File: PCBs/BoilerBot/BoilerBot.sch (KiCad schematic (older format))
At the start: 24 parts, among them J1 Screw_Terminal_01x02, J10 Conn_01x03_Male, J2 Screw_Terminal_01x03, J3 Screw_Terminal_01x03, J4 Screw_Terminal_01x02, J5 Conn_01x05_Male, J6 Conn_01x03_Male, J7 Conn_01x03_Male, J8 Screw_Terminal_01x03, J9 Conn_01x04_Male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

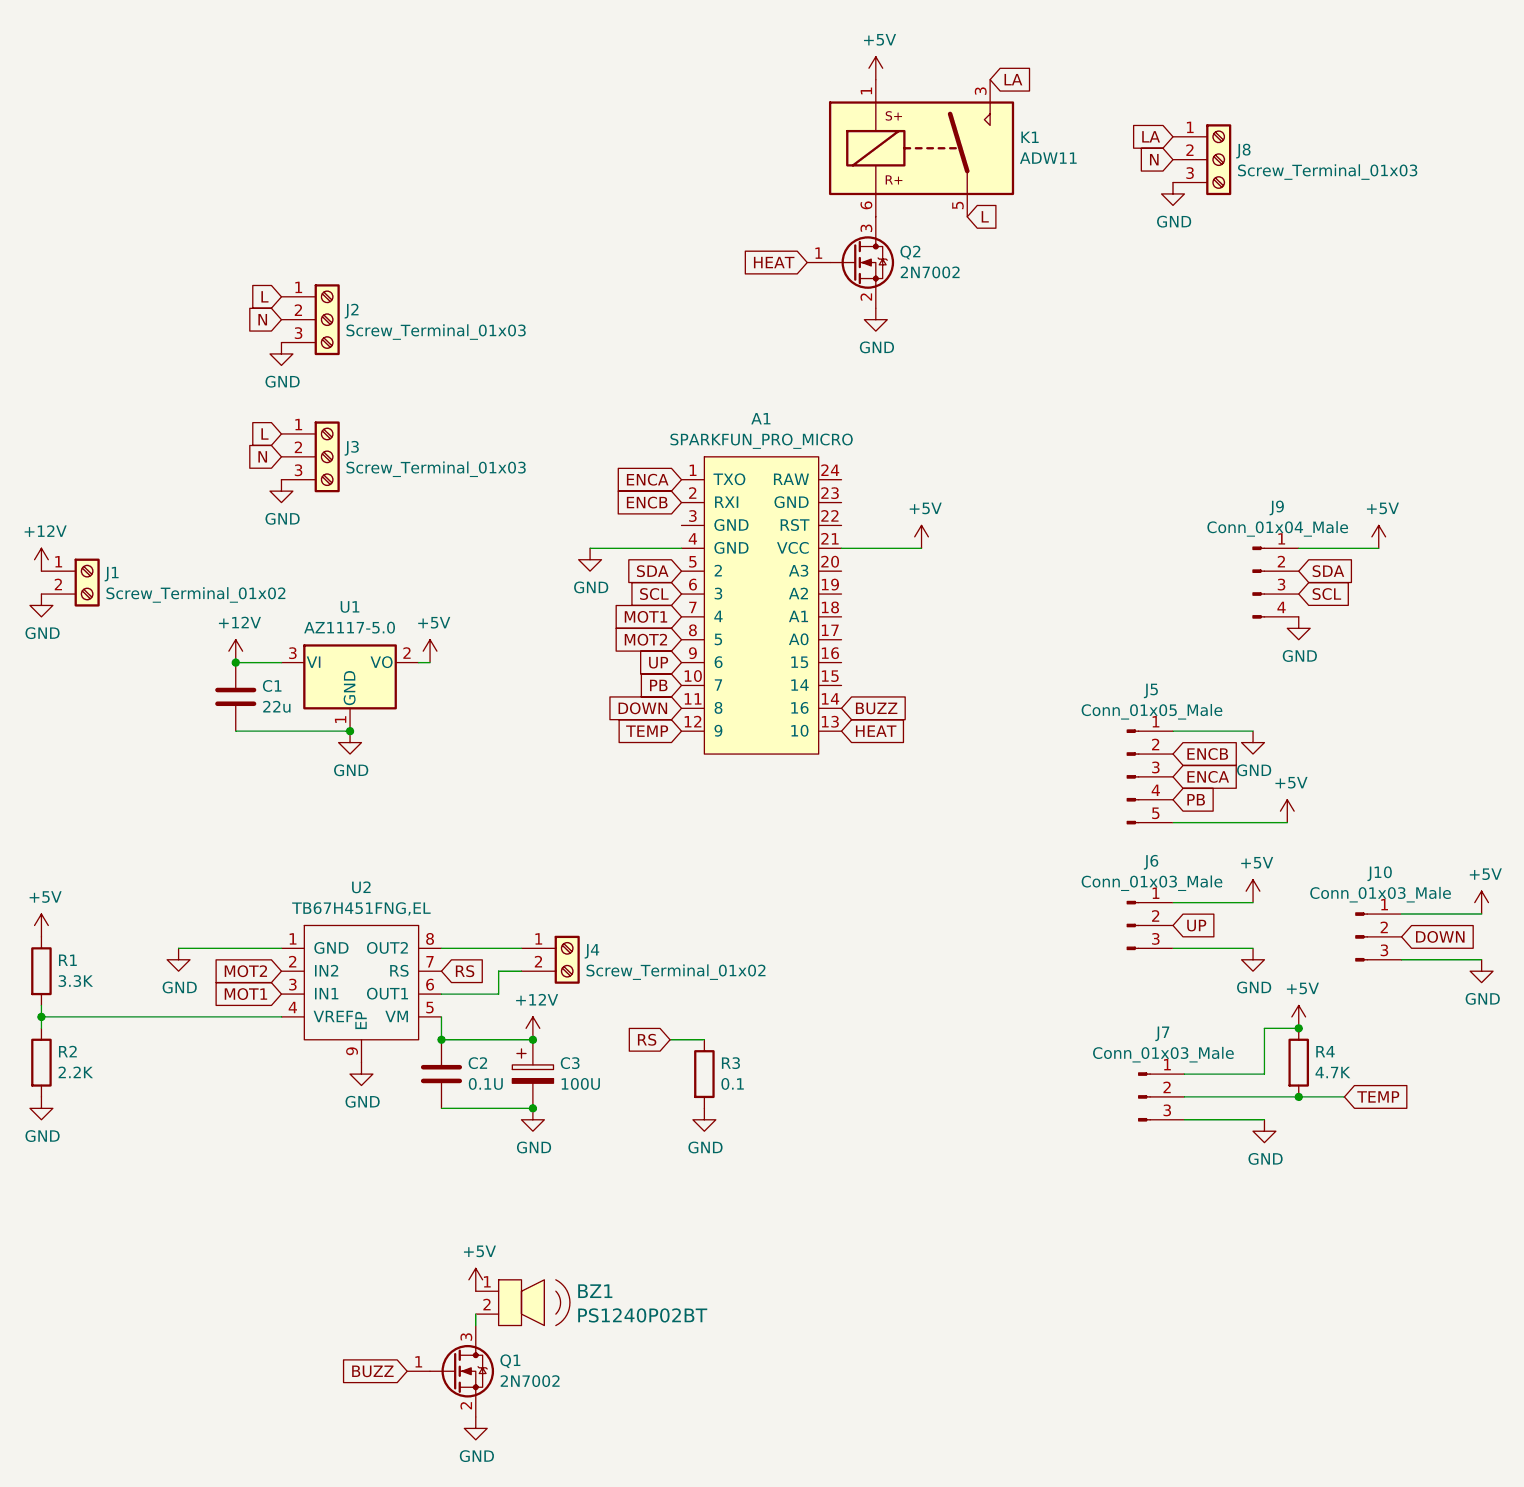
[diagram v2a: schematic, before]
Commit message: updates for off board PDB
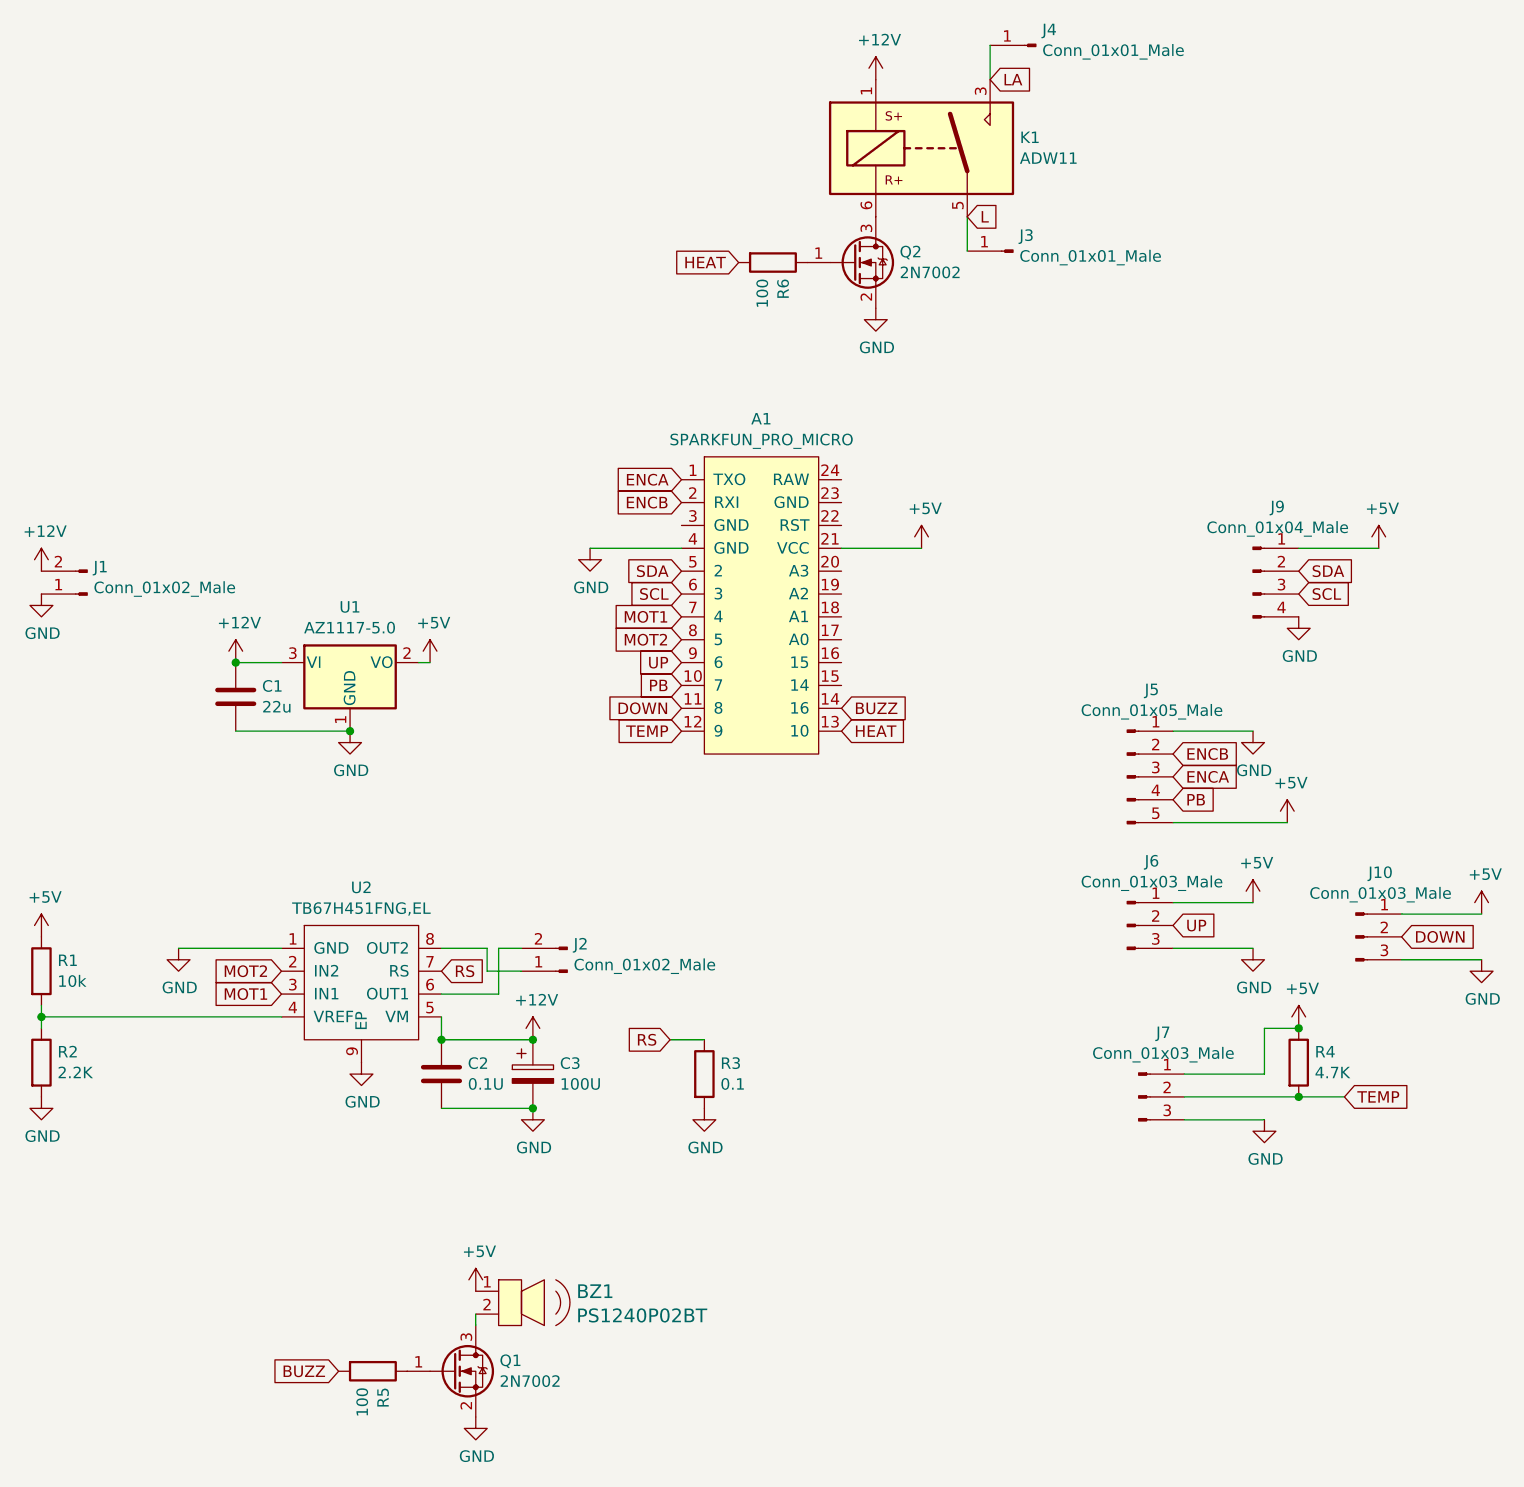
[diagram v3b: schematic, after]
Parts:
- removed J1, J4: Screw_Terminal_01x02, TerminalBlock_Phoenix:TerminalBlock_Phoenix_PT-1,5-2-5.0-H_1x02_P5.00mm_Horizontal, symbol Connector:Screw_Terminal_01x02
- removed J2, J3, J8: Screw_Terminal_01x03, TerminalBlock_Phoenix:TerminalBlock_Phoenix_PT-1,5-3-5.0-H_1x03_P5.00mm_Horizontal, symbol Connector:Screw_Terminal_01x03
- added J1, J2: Conn_01x02_Male, Connector_JST:JST_XH_B2B-XH-A_1x02_P2.50mm_Vertical, symbol Connector:Conn_01x02_Male
- added J3, J4: Conn_01x01_Male, Connector_Wire:SolderWire-2sqmm_1x01_D2mm_OD3.9mm, symbol Connector:Conn_01x01_Male
- added R5, R6: 100, Resistor_SMD:R_0805_2012Metric_Pad1.20x1.40mm_HandSolder, symbol Device:R
- R1: value 3.3K -> 10k
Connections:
- net +12V: now also K1.1, J1.2 (Pin_2)
- net +5V: no longer K1.1
- net BUZZ: now also R5.2; no longer Q1.1 (G)
- net GND: now also J1.1 (Pin_1)
- net HEAT: now also R6.2; no longer Q2.1 (G)
- net L: now also J3.1 (Pin_1)
- net LA: now also J4.1 (Pin_1)
- net at U2.6 (OUT1): now also J2.2 (Pin_2)
- net at U2.8 (OUT2): now also J2.1 (Pin_1)
- new net: Q1.1 (G), R5.1
- new net: Q2.1 (G), R6.1
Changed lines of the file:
@@
 	4800 3600 5200 3600
-$Comp
-L Connector:Screw_Terminal_01x03 J3
-U 1 1 60A388DD
-P 3650 3200
-F 0 "J3" H 3730 3242 50  0000 L CNN
-F 1 "Screw_Terminal_01x03" H 3730 3151 50  0000 L CNN
-F 2 "TerminalBlock_Phoenix:TerminalBlock_Phoenix_PT-1,5-3-5.0-H_1x03_P5.00mm_Horizontal" H 3650 3200 50  0001 C CNN
-F 3 "~" H 3650 3200 50  0001 C CNN
-	1    3650 3200
-	1    0    0    -1
-$EndComp
-Text GLabel 3450 3100 0    50   Input ~ 0
-L
-Text GLabel 3450 3200 0    50   Input ~ 0
-N
-$Comp
-L power:GND #PWR0103
-U 1 1 60A38B35
-P 3450 3300
-F 0 "#PWR0103" H 3450 3050 50  0001 C CNN
-F 1 "GND" H 3455 3127 50  0000 C CNN
-F 2 "" H 3450 3300 50  0001 C CNN
-F 3 "" H 3450 3300 50  0001 C CNN
-	1    3450 3300
-	1    0    0    -1
-$EndComp
 $Comp
 L Regulator_Linear:AZ1117-5.0 U1
@@
 $EndComp
 $Comp
-L Connector:Screw_Terminal_01x02 J1
-U 1 1 60A3A32A
-P 2600 3700
-F 0 "J1" H 2680 3692 50  0000 L CNN
-F 1 "Screw_Terminal_01x02" H 2680 3601 50  0000 L CNN
-F 2 "TerminalBlock_Phoenix:TerminalBlock_Phoenix_PT-1,5-2-5.0-H_1x02_P5.00mm_Horizontal" H 2600 3700 50  0001 C CNN
-F 3 "~" H 2600 3700 50  0001 C CNN
-	1    2600 3700
-	1    0    0    -1
-$EndComp
-$Comp
 L power:+12V #PWR0104
 U 1 1 60A3AB8A
@@
 	4100 4100 4050 4100
 $Comp
-L Connector:Screw_Terminal_01x03 J2
-U 1 1 60A3E6B1
-P 3650 2600
-F 0 "J2" H 3730 2642 50  0000 L CNN
-F 1 "Screw_Terminal_01x03" H 3730 2551 50  0000 L CNN
-F 2 "TerminalBlock_Phoenix:TerminalBlock_Phoenix_PT-1,5-3-5.0-H_1x03_P5.00mm_Horizontal" H 3650 2600 50  0001 C CNN
-F 3 "~" H 3650 2600 50  0001 C CNN
-	1    3650 2600
-	1    0    0    -1
-$EndComp
-Text GLabel 3450 2500 0    50   Input ~ 0
-L
-Text GLabel 3450 2600 0    50   Input ~ 0
-N
-$Comp
-L power:GND #PWR0109
-U 1 1 60A3E6B9
-P 3450 2700
-F 0 "#PWR0109" H 3450 2450 50  0001 C CNN
-F 1 "GND" H 3455 2527 50  0000 C CNN
-F 2 "" H 3450 2700 50  0001 C CNN
-F 3 "" H 3450 2700 50  0001 C CNN
-	1    3450 2700
-	1    0    0    -1
-$EndComp
-$Comp
 L BoilerBot:TB67H451FNG,EL U2
 U 1 1 60A3F0F5
@@
 P 2400 5450
 F 0 "R1" H 2470 5496 50  0000 L CNN
-F 1 "3.3K" H 2470 5405 50  0000 L CNN
+F 1 "10k" H 2470 5405 50  0000 L CNN
 F 2 "Resistor_SMD:R_0805_2012Metric_Pad1.20x1.40mm_HandSolder" V 2330 5450 50  0001 C CNN
 F 3 "~" H 2400 5450 50  0001 C CNN
@@
 	4150 6050 4550 6050
 Connection ~ 4550 6050
-$Comp
-L Connector:Screw_Terminal_01x02 J4
-U 1 1 60A4B537
-P 4700 5350
-F 0 "J4" H 4780 5342 50  0000 L CNN
-F 1 "Screw_Terminal_01x02" H 4780 5251 50  0000 L CNN
-F 2 "TerminalBlock_Phoenix:TerminalBlock_Phoenix_PT-1,5-2-5.0-H_1x02_P5.00mm_Horizontal" H 4700 5350 50  0001 C CNN
-F 3 "~" H 4700 5350 50  0001 C CNN
-	1    4700 5350
-	1    0    0    -1
-$EndComp
-Wire Wire Line
-	4150 5350 4500 5350
-Wire Wire Line
-	4500 5450 4400 5450
-Wire Wire Line
-	4400 5450 4400 5550
 Wire Wire Line
 	4400 5550 4150 5550
@@
 	1    0    0    -1
 $EndComp
-Text GLabel 4000 7200 0    50   Input ~ 0
+Text GLabel 3700 7200 0    50   Input ~ 0
 BUZZ
 $Comp
@@
 $EndComp
 $Comp
-L power:+5V #PWR0130
-U 1 1 60A70017
-P 6050 1550
-F 0 "#PWR0130" H 6050 1400 50  0001 C CNN
-F 1 "+5V" H 6065 1723 50  0000 C CNN
-F 2 "" H 6050 1550 50  0001 C CNN
-F 3 "" H 6050 1550 50  0001 C CNN
-	1    6050 1550
-	1    0    0    -1
-$EndComp
-$Comp
 L Relay:ADW11 K1
 U 1 1 60A7181A
@@
 	1    0    0    -1
 $EndComp
-Text GLabel 5750 2350 0    50   Input ~ 0
+Text GLabel 5450 2350 0    50   Input ~ 0
 HEAT
 Text GLabel 6450 2150 2    50   Input ~ 0
@@
 LA
 $Comp
-L Connector:Screw_Terminal_01x03 J8
-U 1 1 60A76B57
-P 7550 1900
-F 0 "J8" H 7630 1942 50  0000 L CNN
-F 1 "Screw_Terminal_01x03" H 7630 1851 50  0000 L CNN
-F 2 "TerminalBlock_Phoenix:TerminalBlock_Phoenix_PT-1,5-3-5.0-H_1x03_P5.00mm_Horizontal" H 7550 1900 50  0001 C CNN
-F 3 "~" H 7550 1900 50  0001 C CNN
-	1    7550 1900
-	1    0    0    -1
-$EndComp
-Text GLabel 7350 1900 0    50   Input ~ 0
-N
-$Comp
-L power:GND #PWR0131
-U 1 1 60A76B5F
-P 7350 2000
-F 0 "#PWR0131" H 7350 1750 50  0001 C CNN
-F 1 "GND" H 7355 1827 50  0000 C CNN
-F 2 "" H 7350 2000 50  0001 C CNN
-F 3 "" H 7350 2000 50  0001 C CNN
-	1    7350 2000
-	1    0    0    -1
-$EndComp
-Text GLabel 7350 1800 0    50   Input ~ 0
-LA
+L Connector:Conn_01x02_Male J1
+U 1 1 60BA5CAB
+P 2600 3800
+F 0 "J1" H 2572 3682 50  0000 R CNN
+F 1 "Conn_01x02_Male" H 2572 3773 50  0000 R CNN
+F 2 "Connector_JST:JST_XH_B2B-XH-A_1x02_P2.50mm_Vertical" H 2600 3800 50  0001 C CNN
+F 3 "~" H 2600 3800 50  0001 C CNN
+	1    2600 3800
+	-1   0    0    1
+$EndComp
+$Comp
+L Connector:Conn_01x02_Male J2
+U 1 1 60BA6DAD
+P 4700 5450
+F 0 "J2" H 4672 5332 50  0000 R CNN
+F 1 "Conn_01x02_Male" H 4672 5423 50  0000 R CNN
+F 2 "Connector_JST:JST_XH_B2B-XH-A_1x02_P2.50mm_Vertical" H 4700 5450 50  0001 C CNN
+F 3 "~" H 4700 5450 50  0001 C CNN
+	1    4700 5450
+	-1   0    0    1
+$EndComp
+$Comp
+L Device:R R6
+U 1 1 60BA7242
+P 5600 2350
+F 0 "R6" H 5670 2396 50  0000 L CNN
+F 1 "100" H 5670 2305 50  0000 L CNN
+F 2 "Resistor_SMD:R_0805_2012Metric_Pad1.20x1.40mm_HandSolder" V 5530 2350 50  0001 C CNN
+F 3 "~" H 5600 2350 50  0001 C CNN
+	1    5600 2350
+	0    1    1    0
+$EndComp
+$Comp
+L power:+12V #PWR01
+U 1 1 60BA83B8
+P 6050 1550
+F 0 "#PWR01" H 6050 1400 50  0001 C CNN
+F 1 "+12V" H 6065 1723 50  0000 C CNN
+F 2 "" H 6050 1550 50  0001 C CNN
+F 3 "" H 6050 1550 50  0001 C CNN
+	1    6050 1550
+	1    0    0    -1
+$EndComp
+$Comp
+L Device:R R5
+U 1 1 60BA8BA1
+P 3850 7200
+F 0 "R5" H 3920 7246 50  0000 L CNN
+F 1 "100" H 3920 7155 50  0000 L CNN
+F 2 "Resistor_SMD:R_0805_2012Metric_Pad1.20x1.40mm_HandSolder" V 3780 7200 50  0001 C CNN
+F 3 "~" H 3850 7200 50  0001 C CNN
+	1    3850 7200
+	0    1    1    0
+$EndComp
+Wire Wire Line
+	4400 5350 4500 5350
+Wire Wire Line
+	4400 5350 4400 5550
+Wire Wire Line
+	4150 5350 4350 5350
+Wire Wire Line
+	4350 5350 4350 5450
+Wire Wire Line
+	4350 5450 4500 5450
+$Comp
+L Connector:Conn_01x01_Male J3
+U 1 1 60BC6E65
+P 6650 2300
+F 0 "J3" H 6622 2232 50  0000 R CNN
+F 1 "Conn_01x01_Male" H 6622 2323 50  0000 R CNN
+F 2 "Connector_Wire:SolderWire-2sqmm_1x01_D2mm_OD3.9mm" H 6650 2300 50  0001 C CNN
+F 3 "~" H 6650 2300 50  0001 C CNN
+	1    6650 2300
+	-1   0    0    1
+$EndComp
+Wire Wire Line
+	6450 2150 6450 2300
+$Comp
+L Connector:Conn_01x01_Male J4
+U 1 1 60BC8607
+P 6750 1400
+F 0 "J4" H 6722 1332 50  0000 R CNN
+F 1 "Conn_01x01_Male" H 6722 1423 50  0000 R CNN
+F 2 "Connector_Wire:SolderWire-2sqmm_1x01_D2mm_OD3.9mm" H 6750 1400 50  0001 C CNN
+F 3 "~" H 6750 1400 50  0001 C CNN
+	1    6750 1400
+	-1   0    0    1
+$EndComp
+Wire Wire Line
+	6550 1550 6550 1400
 $EndSCHEMATC
